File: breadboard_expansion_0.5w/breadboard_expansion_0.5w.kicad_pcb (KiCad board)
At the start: 2 copper layers, 12.7 x 53.3 mm, 4 parts, among them J1 Conn_01x02_Male, J2 Conn_01x02_Male, J3 Conn_01x02_Male, J4 Conn_01x02_Male

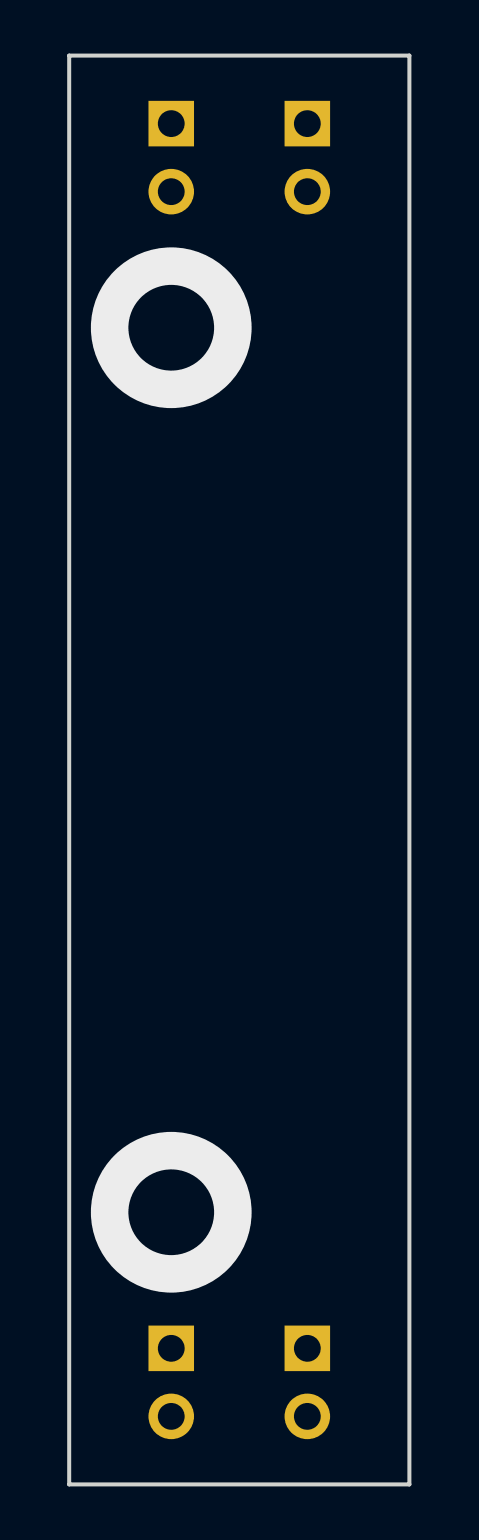
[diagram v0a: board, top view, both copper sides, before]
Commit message: Add voltage labels.
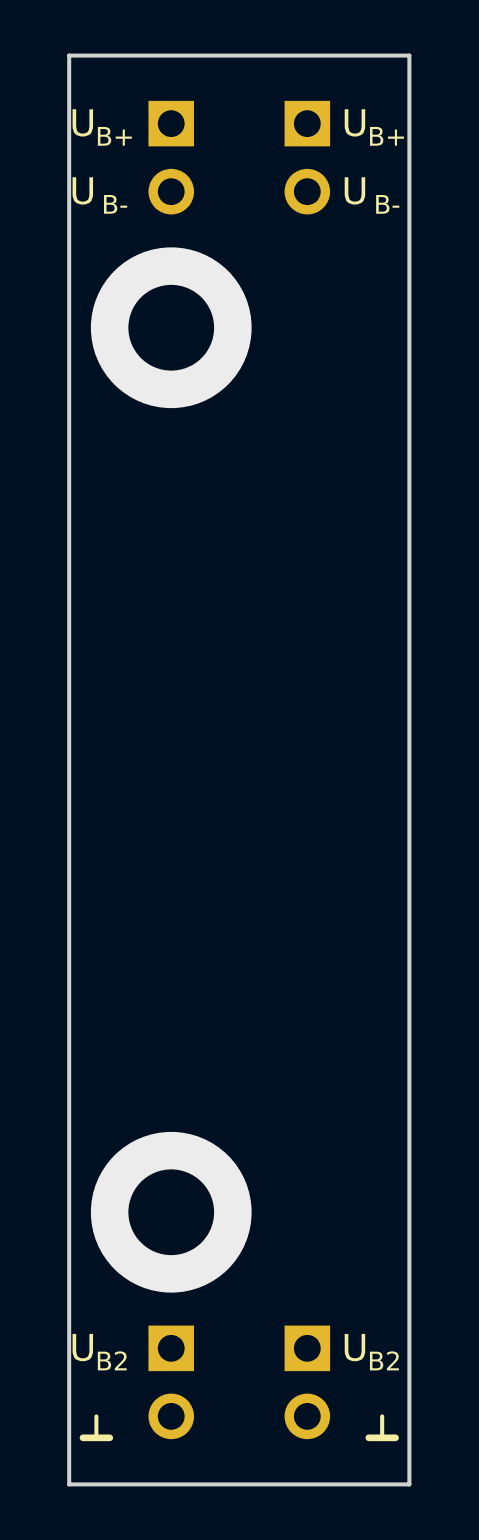
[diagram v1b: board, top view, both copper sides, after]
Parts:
- added REF**: Text_U_B+_Silkscreen, Symbol-emt:Text_U_B+_Silkscreen, F.Cu at (75.4, 91.4)
- added REF**: Text_U_B-_Silkscreen, Symbol-emt:Text_U_B-_Silkscreen, F.Cu at (75.4, 94.0)
- added REF**: Text_U_B+_Silkscreen, Symbol-emt:Text_U_B+_Silkscreen, F.Cu at (85.6, 91.4)
- added REF**: Text_U_B-_Silkscreen, Symbol-emt:Text_U_B-_Silkscreen, F.Cu at (85.6, 94.0)
- added REF**: Text_U_B2_Silkscreen, Symbol-emt:Text_U_B2_Silkscreen, F.Cu at (75.4, 137.2)
- added REF**: Symbol_GND_Silkscreen, Symbol-emt:Symbol_GND_Silkscreen, F.Cu at (75.9, 139.7)
- added REF**: Symbol_GND_Silkscreen, Symbol-emt:Symbol_GND_Silkscreen, F.Cu at (86.6, 139.7)
- added REF**: Text_U_B2_Silkscreen, Symbol-emt:Text_U_B2_Silkscreen, F.Cu at (85.6, 137.2)
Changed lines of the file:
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@@
     (tracks 2)
     (zones 0)
-    (modules 4)
+    (modules 12)
     (nets 5)
   )
@@
     )
   )
+  (module Symbol-emt:Text_U_B+_Silkscreen (layer F.Cu)
+    (at 75.438 91.44)
+    (descr "Voltage Label Betriebsspannung")
+    (tags "Voltage Label Betriebsspannung")
+    (attr virtual)
+    (fp_text reference REF** (at 0 1.65) (layer F.SilkS) hide
+      (effects (font (size 1 1) (thickness 0.15)))
+    )
+    (fp_text value Text_U_B+_Silkscreen (at 0 -1.5) (layer F.Fab) hide
+      (effects (font (size 1 1) (thickness 0.15)))
+    )
+    (fp_text user B+ (at 1.2 0.5) (layer F.SilkS)
+      (effects (font (size 0.7 0.7) (thickness 0.1)))
+    )
+    (fp_text user U (at 0 0) (layer F.SilkS)
+      (effects (font (size 1 1) (thickness 0.15)))
+    )
+  )
+  (module Symbol-emt:Text_U_B-_Silkscreen (layer F.Cu)
+    (at 75.438 93.98)
+    (descr "Voltage Label Betriebsspannung")
+    (tags "Voltage Label Betriebsspannung")
+    (attr virtual)
+    (fp_text reference REF** (at 0 1.65) (layer F.SilkS) hide
+      (effects (font (size 1 1) (thickness 0.15)))
+    )
+    (fp_text value Text_U_B-_Silkscreen (at 0 -1.5) (layer F.Fab) hide
+      (effects (font (size 1 1) (thickness 0.15)))
+    )
+    (fp_text user B- (at 1.2 0.5) (layer F.SilkS)
+      (effects (font (size 0.7 0.7) (thickness 0.1)))
+    )
+    (fp_text user U (at 0 0) (layer F.SilkS)
+      (effects (font (size 1 1) (thickness 0.15)))
+    )
+  )
+  (module Symbol-emt:Text_U_B+_Silkscreen (layer F.Cu)
+    (at 85.598 91.44)
+    (descr "Voltage Label Betriebsspannung")
+    (tags "Voltage Label Betriebsspannung")
+    (attr virtual)
+    (fp_text reference REF** (at 0 1.65) (layer F.SilkS) hide
+      (effects (font (size 1 1) (thickness 0.15)))
+    )
+    (fp_text value Text_U_B+_Silkscreen (at 0 -1.5) (layer F.Fab) hide
+      (effects (font (size 1 1) (thickness 0.15)))
+    )
+    (fp_text user B+ (at 1.2 0.5) (layer F.SilkS)
+      (effects (font (size 0.7 0.7) (thickness 0.1)))
+    )
+    (fp_text user U (at 0 0) (layer F.SilkS)
+      (effects (font (size 1 1) (thickness 0.15)))
+    )
+  )
+  (module Symbol-emt:Text_U_B-_Silkscreen (layer F.Cu)
+    (at 85.598 93.98)
+    (descr "Voltage Label Betriebsspannung")
+    (tags "Voltage Label Betriebsspannung")
+    (attr virtual)
+    (fp_text reference REF** (at 0 1.65) (layer F.SilkS) hide
+      (effects (font (size 1 1) (thickness 0.15)))
+    )
+    (fp_text value Text_U_B-_Silkscreen (at 0 -1.5) (layer F.Fab) hide
+      (effects (font (size 1 1) (thickness 0.15)))
+    )
+    (fp_text user B- (at 1.2 0.5) (layer F.SilkS)
+      (effects (font (size 0.7 0.7) (thickness 0.1)))
+    )
+    (fp_text user U (at 0 0) (layer F.SilkS)
+      (effects (font (size 1 1) (thickness 0.15)))
+    )
+  )
+  (module Symbol-emt:Text_U_B2_Silkscreen (layer F.Cu)
+    (at 75.438 137.16)
+    (descr "Voltage Label Betriebsspannung")
+    (tags "Voltage Label Betriebsspannung")
+    (attr virtual)
+    (fp_text reference REF** (at 0 1.65) (layer F.SilkS) hide
+      (effects (font (size 1 1) (thickness 0.15)))
+    )
+    (fp_text value Text_U_B2_Silkscreen (at 0 -1.5) (layer F.Fab) hide
+      (effects (font (size 1 1) (thickness 0.15)))
+    )
+    (fp_text user B2 (at 1.1 0.5) (layer F.SilkS)
+      (effects (font (size 0.7 0.7) (thickness 0.1)))
+    )
+    (fp_text user U (at 0 0) (layer F.SilkS)
+      (effects (font (size 1 1) (thickness 0.15)))
+    )
+  )
+  (module Symbol-emt:Symbol_GND_Silkscreen (layer F.Cu)
+    (at 75.946 139.7)
+    (descr "Symbol GND")
+    (tags "Symbol GND")
+    (attr virtual)
+    (fp_text reference REF** (at 0 1.6) (layer F.SilkS) hide
+      (effects (font (size 1 1) (thickness 0.15)))
+    )
+    (fp_text value Symbol_GND_Silkscreen (at 0 -0.75) (layer F.Fab) hide
+      (effects (font (size 1 1) (thickness 0.15)))
+    )
+    (fp_line (start 0 0.8) (end 0 0) (layer F.SilkS) (width 0.15))
+    (fp_line (start -0.5 0.8) (end 0.5 0.8) (layer F.SilkS) (width 0.25))
+  )
+  (module Symbol-emt:Symbol_GND_Silkscreen (layer F.Cu)
+    (at 86.614 139.7)
+    (descr "Symbol GND")
+    (tags "Symbol GND")
+    (attr virtual)
+    (fp_text reference REF** (at 0 1.6) (layer F.SilkS) hide
+      (effects (font (size 1 1) (thickness 0.15)))
+    )
+    (fp_text value Symbol_GND_Silkscreen (at 0 -0.75) (layer F.Fab) hide
+      (effects (font (size 1 1) (thickness 0.15)))
+    )
+    (fp_line (start 0 0.8) (end 0 0) (layer F.SilkS) (width 0.15))
+    (fp_line (start -0.5 0.8) (end 0.5 0.8) (layer F.SilkS) (width 0.25))
+  )
+  (module Symbol-emt:Text_U_B2_Silkscreen (layer F.Cu)
+    (at 85.598 137.16)
+    (descr "Voltage Label Betriebsspannung")
+    (tags "Voltage Label Betriebsspannung")
+    (attr virtual)
+    (fp_text reference REF** (at 0 1.65) (layer F.SilkS) hide
+      (effects (font (size 1 1) (thickness 0.15)))
+    )
+    (fp_text value Text_U_B2_Silkscreen (at 0 -1.5) (layer F.Fab) hide
+      (effects (font (size 1 1) (thickness 0.15)))
+    )
+    (fp_text user B2 (at 1.1 0.5) (layer F.SilkS)
+      (effects (font (size 0.7 0.7) (thickness 0.1)))
+    )
+    (fp_text user U (at 0 0) (layer F.SilkS)
+      (effects (font (size 1 1) (thickness 0.15)))
+    )
+  )

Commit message: Increase width of half base format.
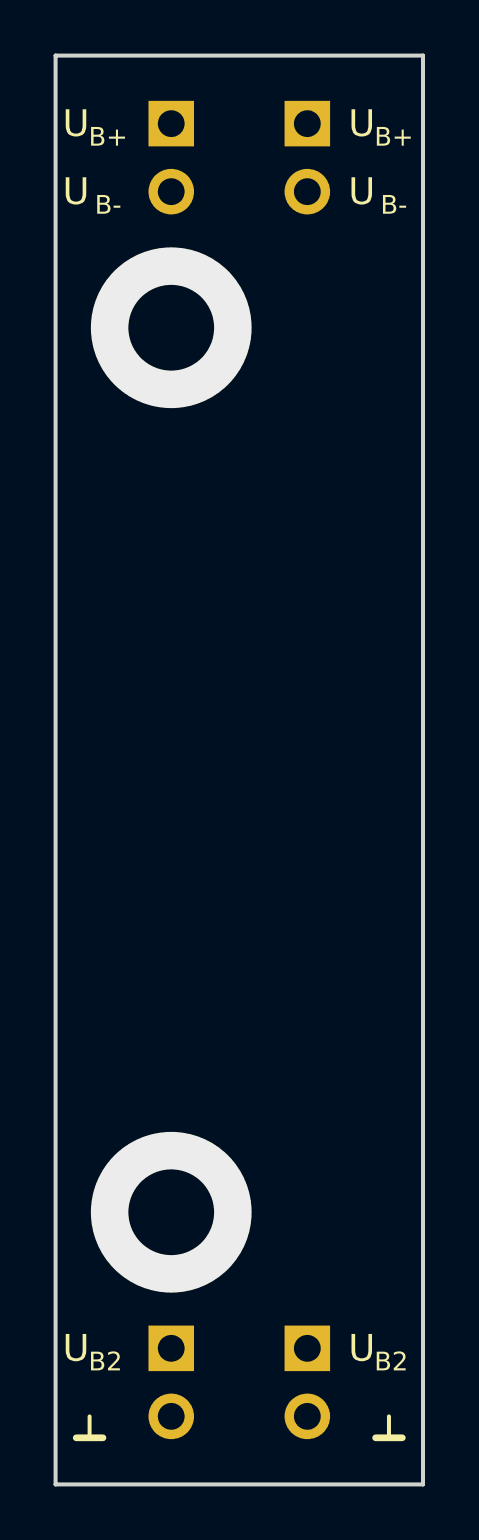
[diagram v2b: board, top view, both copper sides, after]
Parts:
- moved REF** 0.25 mm to (75.2, 91.4)
- moved REF** 0.25 mm to (75.2, 94.0)
- moved REF** 0.25 mm to (85.9, 91.4)
- moved REF** 0.25 mm to (85.9, 94.0)
- moved REF** 0.25 mm to (75.2, 137.2)
- moved REF** 0.25 mm to (75.7, 139.7)
- moved REF** 0.25 mm to (85.9, 137.2)
- moved REF** 0.25 mm to (86.9, 139.7)
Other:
- board size 12.7 x 53.3 mm -> 13.7 x 53.3 mm
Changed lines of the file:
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@@
   )
   (module Symbol-emt:Text_U_B+_Silkscreen (layer F.Cu)
-    (at 75.438 91.44)
+    (at 75.184 91.44)
     (descr "Voltage Label Betriebsspannung")
     (tags "Voltage Label Betriebsspannung")
@@
   )
   (module Symbol-emt:Text_U_B-_Silkscreen (layer F.Cu)
-    (at 75.438 93.98)
+    (at 75.184 93.98)
     (descr "Voltage Label Betriebsspannung")
     (tags "Voltage Label Betriebsspannung")
@@
   )
   (module Symbol-emt:Text_U_B+_Silkscreen (layer F.Cu)
-    (at 85.598 91.44)
+    (at 85.852 91.44)
     (descr "Voltage Label Betriebsspannung")
     (tags "Voltage Label Betriebsspannung")
@@
   )
   (module Symbol-emt:Text_U_B-_Silkscreen (layer F.Cu)
-    (at 85.598 93.98)
+    (at 85.852 93.98)
     (descr "Voltage Label Betriebsspannung")
     (tags "Voltage Label Betriebsspannung")
@@
   )
   (module Symbol-emt:Text_U_B2_Silkscreen (layer F.Cu)
-    (at 75.438 137.16)
+    (at 75.184 137.16)
     (descr "Voltage Label Betriebsspannung")
     (tags "Voltage Label Betriebsspannung")
@@
   )
   (module Symbol-emt:Symbol_GND_Silkscreen (layer F.Cu)
-    (at 75.946 139.7)
+    (at 75.692 139.7)
     (descr "Symbol GND")
     (tags "Symbol GND")
@@
   )
   (module Symbol-emt:Symbol_GND_Silkscreen (layer F.Cu)
-    (at 86.614 139.7)
+    (at 86.868 139.7)
     (descr "Symbol GND")
     (tags "Symbol GND")
@@
   )
   (module Symbol-emt:Text_U_B2_Silkscreen (layer F.Cu)
-    (at 85.598 137.16)
+    (at 85.852 137.16)
     (descr "Voltage Label Betriebsspannung")
     (tags "Voltage Label Betriebsspannung")
@@
     )
   )
-  (gr_line (start 87.63 88.9) (end 87.63 142.24) (layer Edge.Cuts) (width 0.15))
-  (gr_line (start 74.93 142.24) (end 87.63 142.24) (layer Edge.Cuts) (width 0.15))
-  (gr_line (start 74.93 88.9) (end 87.63 88.9) (layer Edge.Cuts) (width 0.15))
-  (gr_line (start 74.93 88.9) (end 74.93 142.24) (layer Edge.Cuts) (width 0.15))
+  (gr_line (start 88.138 88.9) (end 88.138 142.24) (layer Edge.Cuts) (width 0.15))
+  (gr_line (start 74.422 142.24) (end 88.138 142.24) (layer Edge.Cuts) (width 0.15))
+  (gr_line (start 74.422 88.9) (end 88.138 88.9) (layer Edge.Cuts) (width 0.15))
+  (gr_line (start 74.422 88.9) (end 74.422 142.24) (layer Edge.Cuts) (width 0.15))
   (via (at 78.74 99.06) (size 6) (drill 3.2) (layers F.Cu B.Cu) (net 0) (status 40000))
   (via (at 78.74 132.08) (size 6) (drill 3.2) (layers F.Cu B.Cu) (net 0) (status 40000))
